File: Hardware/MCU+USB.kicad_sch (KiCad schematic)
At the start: 2 parts

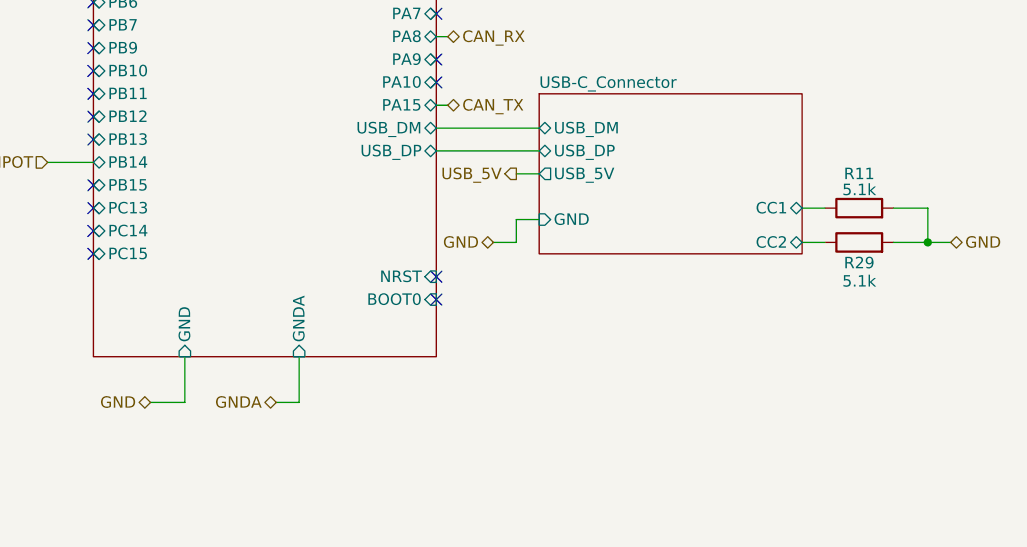
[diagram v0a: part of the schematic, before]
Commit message: Added TestPoints
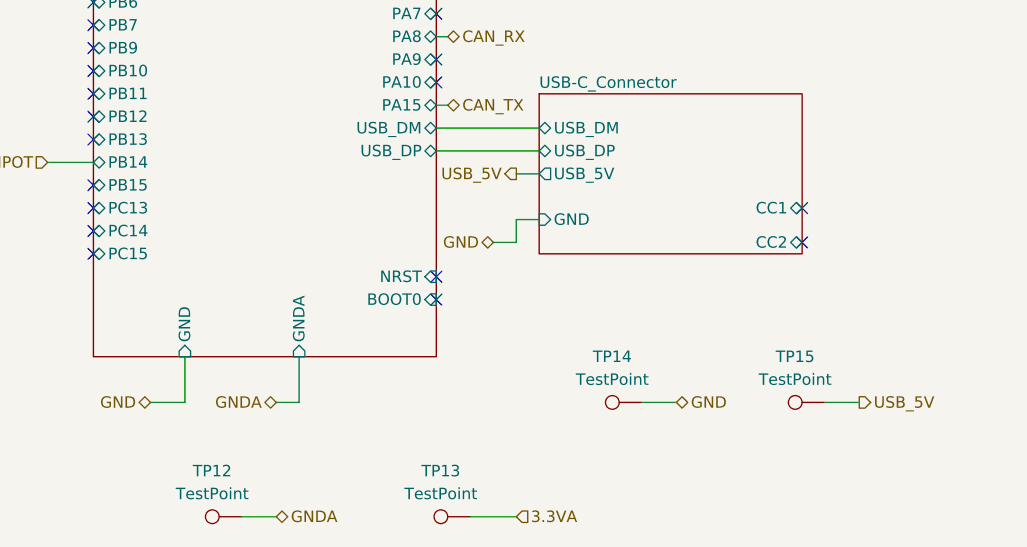
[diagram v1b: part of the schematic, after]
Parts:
- removed R11, R29: 5.1k, symbol Device:R
- added TP12, TP13, TP14, TP15: TestPoint, LHRS_Connectors:Molex_Nano-Fit_105310-xx10_2x05_P2.50mm_Vertical, symbol Connector:TestPoint
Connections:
- net 3.3VA: now also TP13.1
- net GND: now also TP14.1
- net GNDA: now also TP12.1
- net USB_5V: now also TP15.1
- no-connect marks 25 -> 27

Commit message: Final Changes before Final Review
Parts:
- removed TP15: TestPoint, LHRS_Connectors:Molex_Nano-Fit_105310-xx10_2x05_P2.50mm_Vertical, symbol Connector:TestPoint
- TP12: value TestPoint -> GNDA_POINT
- TP13: value TestPoint -> 3.3VA_POINT
- TP14: value TestPoint -> GND_POINT
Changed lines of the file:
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@@
 	)
 	(no_connect
-		(at 144.78 91.44)
+		(at 144.78 80.01)
 	)
 	(no_connect
@@
 	)
 	(no_connect
-		(at 144.78 87.63)
+		(at 144.78 76.2)
 	)
 	(no_connect
@@
 	(wire
 		(pts
-			(xy 113.03 88.9) (xy 113.03 91.44)
+			(xy 88.9 104.14) (xy 88.9 109.22)
 		)
 		(stroke
@@
 	(wire
 		(pts
-			(xy 88.9 104.14) (xy 88.9 109.22)
+			(xy 148.59 83.82) (xy 144.78 83.82)
 		)
 		(stroke
@@
 	(wire
 		(pts
-			(xy 113.03 83.82) (xy 115.57 83.82)
+			(xy 77.47 38.1) (xy 77.47 43.18)
 		)
 		(stroke
@@
 	(wire
 		(pts
-			(xy 77.47 38.1) (xy 77.47 43.18)
+			(xy 144.78 90.17) (xy 148.59 90.17)
 		)
 		(stroke
@@
 	(wire
 		(pts
-			(xy 113.03 88.9) (xy 115.57 88.9)
-		)
-		(stroke
-			(width 0)
-			(type default)
-		)
-	)
-	(wire
-		(pts
 			(xy 76.2 104.14) (xy 76.2 109.22)
 		)
@@
 	(wire
 		(pts
-			(xy 113.03 91.44) (xy 110.49 91.44)
-		)
-		(stroke
-			(width 0)
-			(type default)
-		)
-	)
-	(wire
-		(pts
 			(xy 105.41 68.58) (xy 104.14 68.58)
 		)
@@
 	(wire
 		(pts
-			(xy 147.32 109.22) (xy 151.13 109.22)
-		)
-		(stroke
-			(width 0)
-			(type default)
-		)
-	)
-	(wire
-		(pts
 			(xy 78.74 38.1) (xy 77.47 38.1)
 		)
@@
 	(hierarchical_label "GND"
 		(shape bidirectional)
-		(at 110.49 91.44 180)
+		(at 148.59 90.17 0)
 		(effects
 			(font
 				(size 1.27 1.27)
 			)
-			(justify right)
+			(justify left)
 		)
 	)
@@
 		)
 	)
-	(hierarchical_label "USB_5V"
-		(shape output)
-		(at 151.13 109.22 0)
-		(effects
-			(font
-				(size 1.27 1.27)
-			)
-			(justify left)
-		)
-	)
 	(hierarchical_label "GND"
 		(shape bidirectional)
@@
 	(hierarchical_label "USB_5V"
 		(shape output)
-		(at 113.03 83.82 180)
+		(at 148.59 83.82 0)
 		(effects
 			(font
 				(size 1.27 1.27)
 			)
-			(justify right)
+			(justify left)
 		)
 	)
@@
 	(symbol
 		(lib_id "Connector:TestPoint")
-		(at 147.32 109.22 90)
-		(unit 1)
-		(body_style 1)
-		(exclude_from_sim no)
-		(in_bom yes)
-		(on_board yes)
-		(in_pos_files yes)
-		(dnp no)
-		(fields_autoplaced yes)
-		(property "Reference" "TP15"
-			(at 144.018 104.14 90)
-			(show_name no)
-			(do_not_autoplace no)
-			(effects
-				(font
-					(size 1.27 1.27)
-				)
-			)
-		)
-		(property "Value" "TestPoint"
-			(at 144.018 106.68 90)
-			(show_name no)
-			(do_not_autoplace no)
-			(effects
-				(font
-					(size 1.27 1.27)
-				)
-			)
-		)
-		(property "Footprint" "LHRS_Connectors:Molex_Nano-Fit_105310-xx10_2x05_P2.50mm_Vertical"
-			(at 147.32 104.14 0)
-			(hide yes)
-			(show_name no)
-			(do_not_autoplace no)
-			(effects
-				(font
-					(size 1.27 1.27)
-				)
-			)
-		)
-		(property "Datasheet" ""
-			(at 147.32 104.14 0)
-			(hide yes)
-			(show_name no)
-			(do_not_autoplace no)
-			(effects
-				(font
-					(size 1.27 1.27)
-				)
-			)
-		)
-		(property "Description" "test point"
-			(at 147.32 109.22 0)
-			(hide yes)
-			(show_name no)
-			(do_not_autoplace no)
-			(effects
-				(font
-					(size 1.27 1.27)
-				)
-			)
-		)
-		(pin "1"
-		)
-		(instances
-			(project "SuspensionBoard"
-				(path "/f9dc491a-b8c6-4623-9728-13837ac4bba3/a17e150d-c0ca-4b81-ac9f-0470beae7874"
-					(reference "TP15")
-					(unit 1)
-				)
-			)
-		)
-	)
-	(symbol
-		(lib_id "Connector:TestPoint")
 		(at 127 109.22 90)
 		(unit 1)
@@
 			)
 		)
-		(property "Value" "TestPoint"
+		(property "Value" "GND_POINT"
 			(at 123.698 106.68 90)
 			(show_name no)
@@
 			)
 		)
-		(property "Value" "TestPoint"
+		(property "Value" "3.3VA_POINT"
 			(at 104.648 119.38 90)
 			(show_name no)
@@
 			)
 		)
-		(property "Value" "TestPoint"
+		(property "Value" "GNDA_POINT"
 			(at 79.248 119.38 90)
 			(show_name no)
@@
 		)
 		(pin "CC1" bidirectional
-			(at 144.78 87.63 0)
+			(at 144.78 76.2 0)
 			(effects
 				(font
@@
 		)
 		(pin "CC2" bidirectional
-			(at 144.78 91.44 0)
+			(at 144.78 80.01 0)
 			(effects
 				(font
@@
 		)
 		(pin "GND" input
-			(at 115.57 88.9 180)
+			(at 144.78 90.17 0)
 			(effects
 				(font
 					(size 1.27 1.27)
 				)
-				(justify left)
+				(justify right)
 			)
 		)
 		(pin "USB_5V" output
-			(at 115.57 83.82 180)
+			(at 144.78 83.82 0)
 			(effects
 				(font
 					(size 1.27 1.27)
 				)
-				(justify left)
+				(justify right)
 			)
 		)

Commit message: Final Review Ready
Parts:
- added D15, D16, D17: LED, LED_SMD:LED_0603_1608Metric_Pad1.05x0.95mm_HandSolder, symbol lhrs_misc:Blue_LED
- added R27, R28, R34: 1k, Package_SO:SOIC-14_3.9x8.7mm_P1.27mm, symbol Device:R
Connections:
- net 48PinMCU/PB11: now also R28.1
- net 48PinMCU/PB13: now also R27.1
- net 48PinMCU/PB15: now also R34.1
- net GND: now also D15.1 (K), D16.1 (K), D17.1 (K)
- new net: D16.2 (A), R34.2
- new net: D17.2 (A), R28.2
- new net: D15.2 (A), R27.2
- no-connect marks 27 -> 24
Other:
- note added: "Test_Points"
- moved on the sheet: TP12, TP13, TP14

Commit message: Updated KiCAD Sharepoint
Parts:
- D17: value LED -> HB
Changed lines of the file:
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@@
 	)
 	(hierarchical_label "CAN_RX"
-		(shape bidirectional)
+		(shape input)
 		(at 105.41 68.58 0)
 		(effects
@@
 	)
 	(hierarchical_label "CAN_TX"
-		(shape bidirectional)
+		(shape output)
 		(at 105.41 76.2 0)
 		(effects
@@
 			)
 		)
-		(property "Value" "LED"
+		(property "Value" "HB"
 			(at 35.56 76.454 0)
 			(show_name no)

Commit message: Final Changes without Footprints
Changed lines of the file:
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@@
 	)
 	(no_connect
-		(at 144.78 80.01)
+		(at 144.78 81.28)
 	)
 	(no_connect
@@
 	)
 	(no_connect
-		(at 144.78 76.2)
+		(at 144.78 78.74)
 	)
 	(no_connect
@@
 	(wire
 		(pts
-			(xy 144.78 90.17) (xy 148.59 90.17)
+			(xy 144.78 86.36) (xy 148.59 86.36)
 		)
 		(stroke
@@
 	(hierarchical_label "GND"
 		(shape bidirectional)
-		(at 148.59 90.17 0)
+		(at 148.59 86.36 0)
 		(effects
 			(font
@@
 	)
 	(sheet
-		(at 115.57 74.93)
-		(size 29.21 17.78)
+		(at 115.57 76.2)
+		(size 29.21 12.7)
 		(exclude_from_sim no)
 		(in_bom yes)
@@
 		)
 		(property "Sheetname" "USB-C_Connector"
-			(at 115.57 74.422 0)
+			(at 115.57 75.692 0)
 			(show_name no)
 			(do_not_autoplace no)
@@
 		)
 		(property "Sheetfile" "USB-C_Connector.kicad_sch"
-			(at 115.57 93.218 0)
+			(at 115.57 94.488 0)
 			(hide yes)
 			(show_name no)
@@
 		)
 		(property "Author" "Shuopu Wang"
-			(at 87.63 -55.88 0)
+			(at 87.63 -54.61 0)
 			(hide yes)
 			(show_name no)
@@
 		)
 		(property "Date Modified" "9/5/2026"
-			(at 87.63 -55.88 0)
+			(at 87.63 -54.61 0)
 			(hide yes)
 			(show_name no)
@@
 		)
 		(pin "CC1" bidirectional
-			(at 144.78 76.2 0)
+			(at 144.78 78.74 0)
 			(effects
 				(font
@@
 		)
 		(pin "CC2" bidirectional
-			(at 144.78 80.01 0)
+			(at 144.78 81.28 0)
 			(effects
 				(font
@@
 		)
 		(pin "GND" input
-			(at 144.78 90.17 0)
+			(at 144.78 86.36 0)
 			(effects
 				(font
